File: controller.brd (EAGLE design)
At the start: 100 x 100 mm, 51 parts, among them IC1 7805DT, Q2 MOSFET-NCHANNELBSS123LT1G, Q3 MOSFET-NCHANNELFDD8780, U1 ATMEGA328P, Y1 16MHz

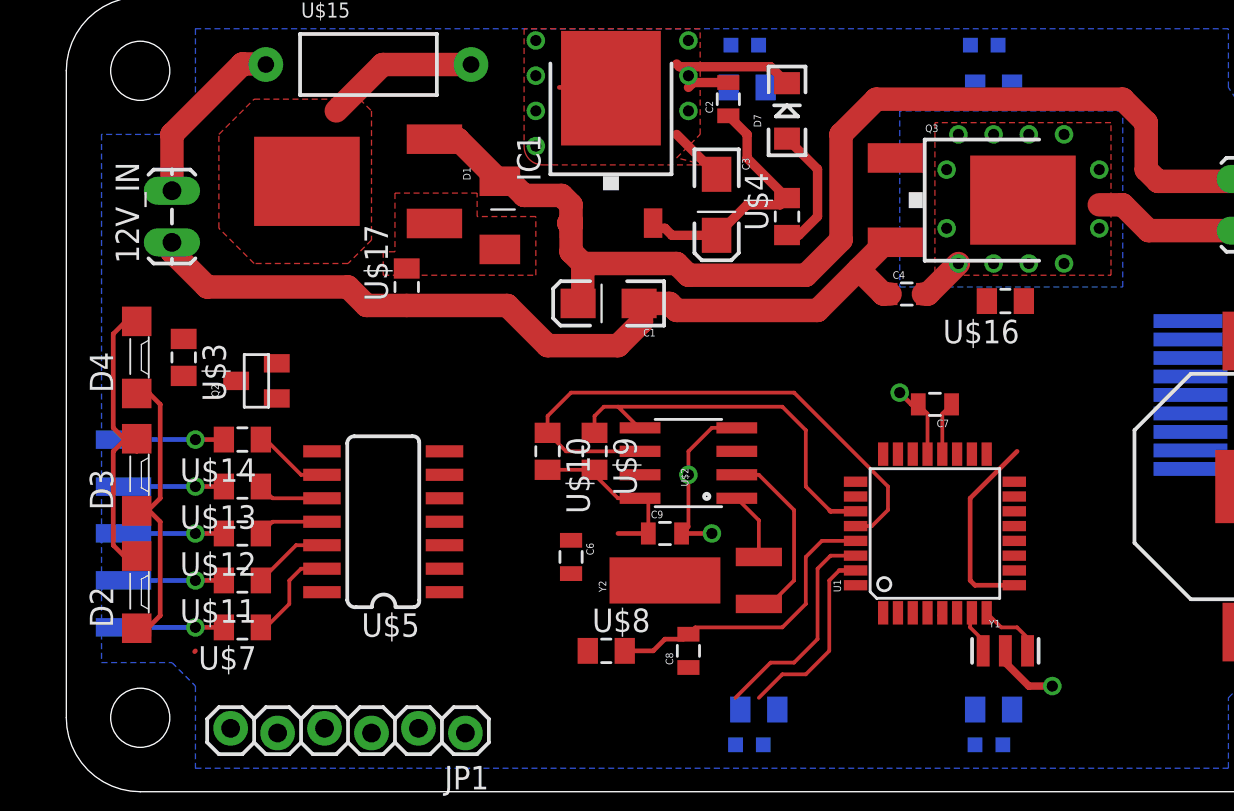
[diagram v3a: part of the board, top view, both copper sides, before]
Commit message: added current limit resistors. tightened rtc-mcu spacing.
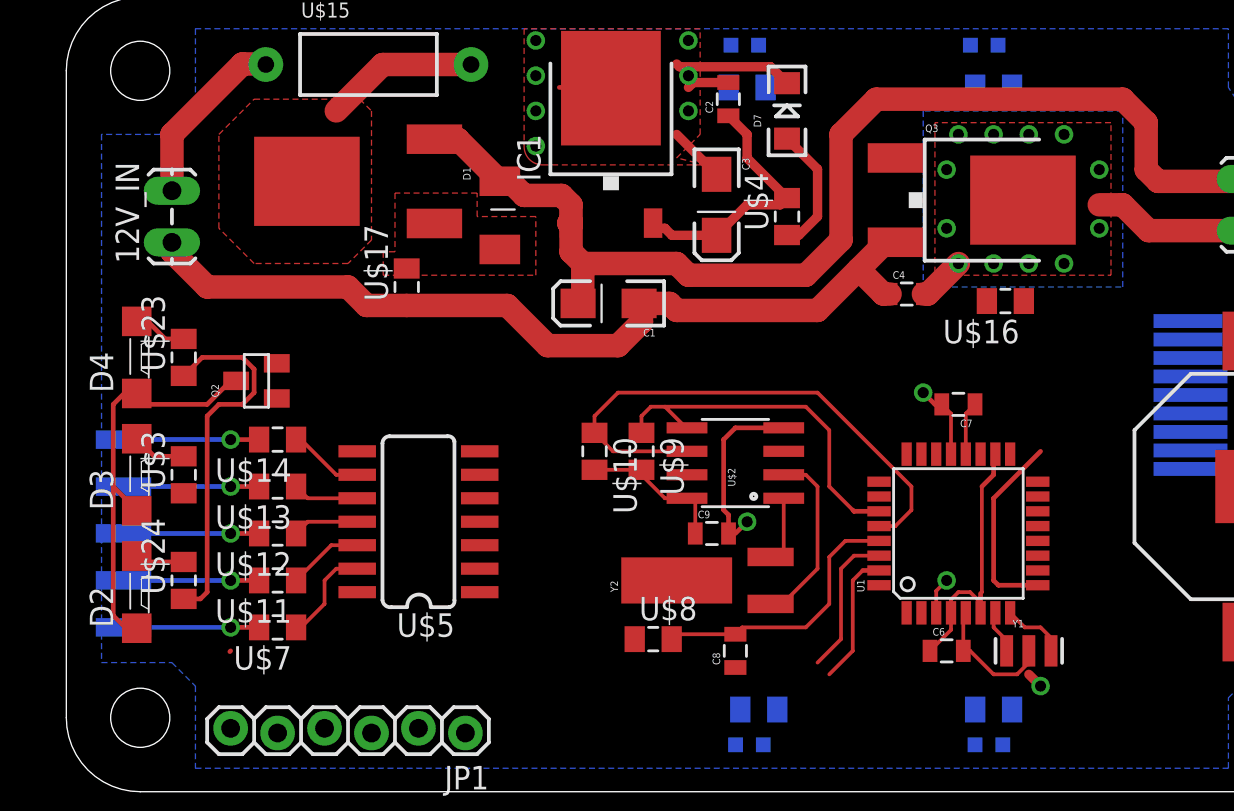
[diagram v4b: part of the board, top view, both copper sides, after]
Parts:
- added U$23, U$24: (no value), jt_parts:RESISTOR-0805
- moved C6 20.9 mm to (52.1, 11.4), turned to 0 degrees
- moved U$3 6.35 mm to (10.8, 21.0), turned to 90 degrees
- moved U$8 2.62 mm to (36.2, 12.1)
- moved U$10 2.54 mm to (33.0, 22.2)
- moved C8 2.54 mm to (40.6, 11.4)
- moved C9 2.54 mm to (39.4, 17.8)
- moved U$2 2.54 mm to (40.6, 21.6)
- moved U$9 2.54 mm to (35.6, 22.2)
- moved U$5 1.91 mm to (23.5, 17.8)
- moved U$11 1.90 mm to (15.9, 15.2)
- moved U$12 1.90 mm to (15.9, 17.8)
- moved U$13 1.90 mm to (15.9, 20.3)
- moved U$14 1.90 mm to (15.9, 22.9)
- moved U$7 1.90 mm to (15.9, 12.7)
- moved Y1 1.27 mm to (56.5, 11.4)
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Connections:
- removed net N$39: U$18.1, U$21.1, U$22.1, U$6.1
- new net N$36: D2.A, U$24.2
- new net N$37: D4.A, U$23.2
- net 12V: now also U$18.1, U$21.1, U$22.1, U$23.1, U$24.1, U$3.1, U$6.1
- net 5V: no longer U$3.1
- net N$9: no longer D2.A, D4.A
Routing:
- net 12V: track 62.9 -> 82.6 mm
- net N$9: track 17.0 -> 2.93 mm
- net 5V: track 23.9 -> 37.0 mm
- net GND: track 85.2 -> 91.7 mm
- net N$12: track 17.8 -> 22.5 mm
- net RXI: track 11.9 -> 7.96 mm
- net N$37: track 0.00 -> 3.38 mm
- net TXO: track 10.3 -> 7.25 mm
- net N$36: track 0.00 -> 2.67 mm
- net N$31: track 5.43 -> 7.33 mm
- net N$30: track 5.43 -> 7.33 mm
- net N$29: track 5.43 -> 7.33 mm
- net N$28: track 5.43 -> 7.33 mm
- net N$21: track 5.43 -> 7.33 mm
- net N$15: track 16.4 -> 14.9 mm
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
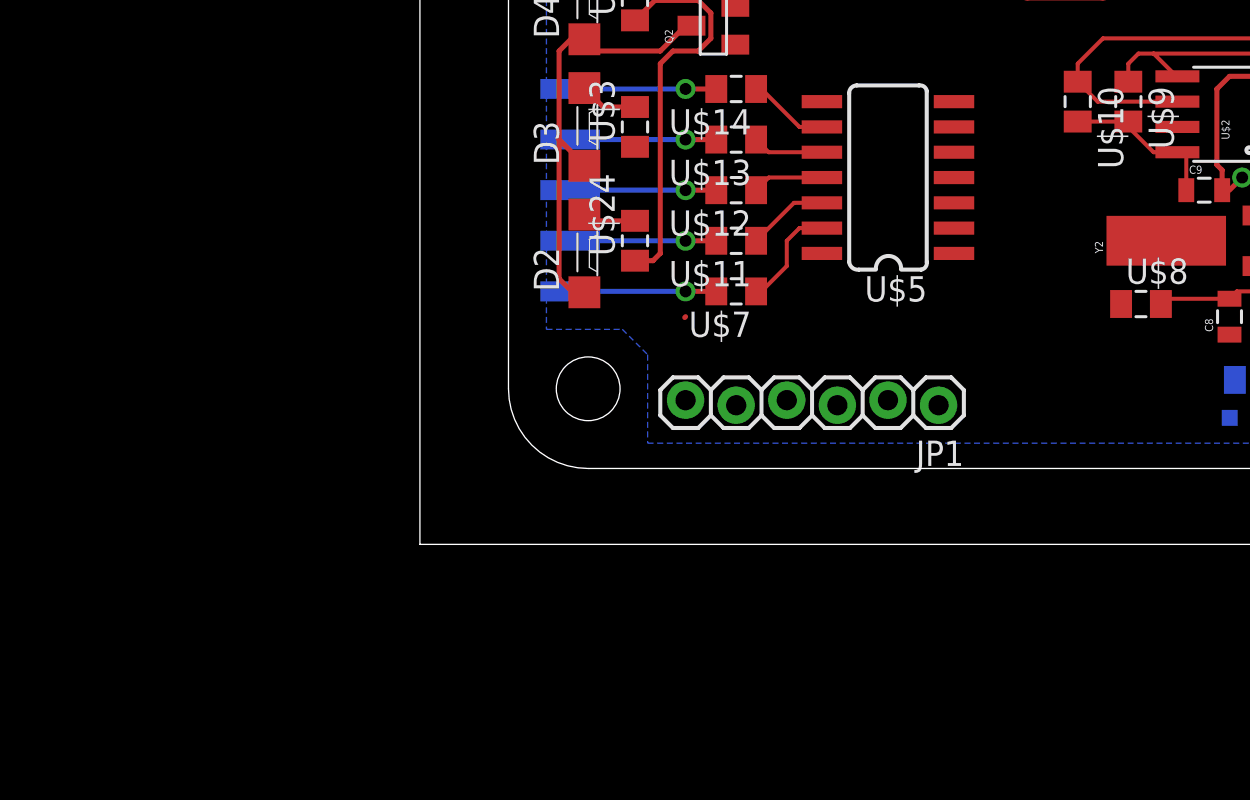
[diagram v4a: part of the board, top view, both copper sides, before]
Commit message: wired lcd for software reset.
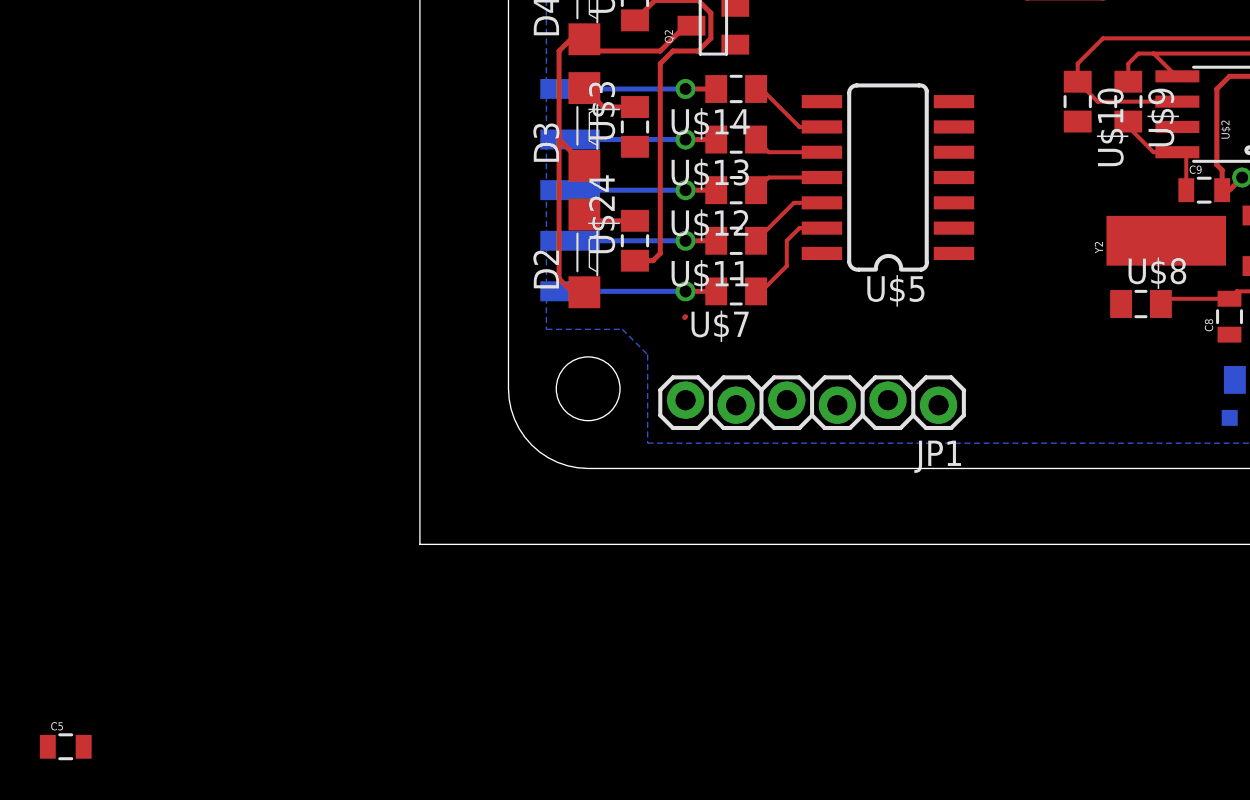
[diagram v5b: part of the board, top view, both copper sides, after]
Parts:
- added C5: (no value), SparkFun-Capacitors:0805
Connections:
- net N$17 renamed D/C
- net N$19 renamed /RES
- net N$2 renamed SDIN
- net N$5 renamed SCLK
- removed net N$18: NOKIA5110.5
- new net VCC: NOKIA5110.1, NOKIA5110.6, U$10.2, U$9.2
- net 5V: no longer NOKIA5110.1, U$10.2, U$9.2
- net GND: now also C5.1, NOKIA5110.5
- net N$20: now also C5.2, NOKIA5110.8; no longer NOKIA5110.6
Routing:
- net 5V: track 37.0 -> 34.2 mm
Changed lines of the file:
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@@
 <element name="U$23" library="jt_parts" package="RESISTOR-0805" value="" x="10.795" y="27.305" rot="R90"/>
 <element name="U$24" library="jt_parts" package="RESISTOR-0805" value="" x="10.795" y="15.24" rot="R90"/>
+<element name="C5" library="SparkFun-Capacitors" package="0805" value="" x="-17.78" y="-10.16"/>
 </elements>
 <signals>
@@
 <wire x1="51.505" y1="13.4874" x2="51.505" y2="14.675" width="0.2032" layer="1"/>
 <wire x1="51.505" y1="14.675" x2="52.07" y2="15.24" width="0.2032" layer="1"/>
-<wire x1="65.26" y1="23.273" x2="68.58" y2="20.32" width="0" layer="19" extent="1-16"/>
-<wire x1="40.27" y1="17.78" x2="40.64" y2="17.78" width="0" layer="19" extent="1-1"/>
-<wire x1="13.292" y1="11.387" x2="13.335" y2="7.239" width="0" layer="19" extent="1-1"/>
-<wire x1="15.832" y1="26.985" x2="12.065" y2="31.115" width="0" layer="19" extent="1-1"/>
-<wire x1="56.245" y1="30.353" x2="49.011" y2="30.734" width="0" layer="19" extent="1-1"/>
-<wire x1="26.8097" y1="14.605" x2="40.27" y2="17.78" width="0" layer="19" extent="1-1"/>
 <wire x1="43.2562" y1="23.495" x2="40.64" y2="23.495" width="0.254" layer="1"/>
 <wire x1="40.64" y1="23.495" x2="40.005" y2="22.86" width="0.254" layer="1"/>
@@
 <wire x1="40.27" y1="18.785" x2="40.005" y2="19.05" width="0.254" layer="1"/>
 <wire x1="57.15" y1="9.525" x2="56.515" y2="10.16" width="0.508" layer="1"/>
-<wire x1="56.515" y1="10.16" x2="56.1975" y2="10.4775" width="0" layer="19" extent="1-16"/>
+<contactref element="NOKIA5110" pad="5"/>
+<contactref element="C5" pad="1"/>
+<wire x1="43.434" y1="42.14" x2="54.852" y2="44.196" width="0" layer="19" extent="1-16"/>
+<wire x1="38.1" y1="42.545" x2="37.616" y2="43.029" width="0" layer="19" extent="1-1"/>
+<wire x1="38.365" y1="42.175" x2="38.1" y2="42.545" width="0" layer="19" extent="1-1"/>
+<wire x1="38.1" y1="40.64" x2="38.1" y2="41.91" width="0" layer="19" extent="1-1"/>
+<wire x1="41.898" y1="44.196" x2="42.545" y2="43.029" width="0" layer="19" extent="1-16"/>
+<wire x1="38.1" y1="44.45" x2="37.465" y2="43.18" width="0" layer="19" extent="1-1"/>
+<wire x1="37.465" y1="39.369" x2="38.1" y2="40.64" width="0" layer="19" extent="1-1"/>
+<wire x1="36.195" y1="39.37" x2="37.465" y2="39.369" width="0" layer="19" extent="1-1"/>
+<wire x1="29.845" y1="42.545" x2="31.115" y2="41.91" width="0" layer="19" extent="1-1"/>
+<wire x1="29.845" y1="40.64" x2="31.115" y2="41.91" width="0" layer="19" extent="1-1"/>
+<wire x1="29.845" y1="44.45" x2="29.845" y2="42.545" width="0" layer="19" extent="1-1"/>
+<wire x1="29.845" y1="38.735" x2="29.845" y2="40.64" width="0" layer="19" extent="1-1"/>
+<wire x1="37.084" y1="30.226" x2="39.624" y2="37.21" width="0" layer="19" extent="1-1"/>
+<wire x1="15.832" y1="26.985" x2="12.065" y2="31.115" width="0" layer="19" extent="1-1"/>
+<wire x1="50.8" y1="25.4" x2="49.011" y2="30.734" width="0" layer="19" extent="1-1"/>
+<wire x1="43.2562" y1="23.495" x2="45.085" y2="29.845" width="0" layer="19" extent="1-1"/>
+<wire x1="40.64" y1="17.78" x2="40.27" y2="17.78" width="0" layer="19" extent="1-1"/>
+<wire x1="52.07" y1="15.24" x2="52.305" y2="22.0726" width="0" layer="19" extent="1-1"/>
+<wire x1="52.97" y1="13.3524" x2="51.505" y2="13.4874" width="0" layer="19" extent="1-1"/>
+<wire x1="56.515" y1="10.16" x2="56.515" y2="10.795" width="0" layer="19" extent="1-1"/>
+<wire x1="55.106" y1="6.35" x2="57.15" y2="9.525" width="0" layer="19" extent="16-16"/>
+<wire x1="56.245" y1="30.353" x2="51.805" y2="24.765" width="0" layer="19" extent="1-1"/>
+<wire x1="65.26" y1="25.273" x2="56.245" y2="30.353" width="0" layer="19" extent="1-16"/>
+<wire x1="65.26" y1="23.273" x2="65.26" y2="25.273" width="0" layer="19" extent="16-16"/>
+<wire x1="68.58" y1="20.32" x2="65.26" y2="23.273" width="0" layer="19" extent="1-16"/>
+<wire x1="42.152" y1="6.35" x2="40.64" y2="17.78" width="0" layer="19" extent="1-16"/>
+<wire x1="26.8097" y1="14.605" x2="30.48" y2="27.94" width="0" layer="19" extent="1-1"/>
+<wire x1="15.875" y1="6.985" x2="26.8097" y2="14.605" width="0" layer="19" extent="1-1"/>
+<wire x1="13.335" y1="7.239" x2="15.875" y2="6.985" width="0" layer="19" extent="1-1"/>
+<wire x1="13.292" y1="11.387" x2="13.335" y2="7.239" width="0" layer="19" extent="1-1"/>
+<wire x1="-18.68" y1="-10.16" x2="13.335" y2="7.239" width="0" layer="19" extent="1-1"/>
 </signal>
 <signal name="5V" class="2">
@@
 <contactref element="C9" pad="1"/>
 <contactref element="U$2" pad="8"/>
-<contactref element="U$9" pad="2"/>
-<contactref element="U$10" pad="2"/>
-<wire x1="33.02" y1="21.225" x2="35.56" y2="21.225" width="0.2032" layer="1"/>
-<wire x1="35.56" y1="21.225" x2="35.56" y2="20.955" width="0.2032" layer="1"/>
 <wire x1="35.56" y1="20.955" x2="36.83" y2="19.685" width="0.2032" layer="1"/>
 <wire x1="36.83" y1="19.685" x2="38.0238" y2="19.685" width="0.2032" layer="1"/>
 <wire x1="38.0238" y1="19.685" x2="38.47" y2="19.685" width="0.2032" layer="1"/>
 <wire x1="38.47" y1="19.685" x2="38.47" y2="17.78" width="0.2032" layer="1"/>
-<contactref element="NOKIA5110" pad="1"/>
 <wire x1="40.259" y1="40.375" x2="40.27" y2="40.375" width="0.508" layer="1"/>
 <wire x1="40.27" y1="40.375" x2="41.275" y2="39.37" width="0.508" layer="1"/>
@@
 <wire x1="54.61" y1="20.955" x2="54.61" y2="21.9776" width="0.254" layer="1"/>
 <wire x1="54.61" y1="21.9776" x2="54.705" y2="22.0726" width="0.2032" layer="1"/>
-<wire x1="54.705" y1="22.0726" x2="65.26" y2="29.273" width="0" layer="19" extent="1-16"/>
-<wire x1="38.47" y1="17.78" x2="51.17" y2="11.43" width="0" layer="19" extent="1-1"/>
-<wire x1="35.195" y1="12.065" x2="38.47" y2="17.78" width="0" layer="19" extent="1-1"/>
-<wire x1="20.1803" y1="14.605" x2="33.02" y2="21.225" width="0" layer="19" extent="1-1"/>
-<wire x1="18.415" y1="7.239" x2="20.1803" y2="14.605" width="0" layer="19" extent="1-1"/>
-<wire x1="37.21" y1="33.91" x2="35.56" y2="21.225" width="0" layer="19" extent="1-1"/>
 <wire x1="52.305" y1="13.4874" x2="52.305" y2="12.565" width="0.2032" layer="1"/>
 <wire x1="52.305" y1="12.565" x2="51.17" y2="11.43" width="0.2032" layer="1"/>
+<wire x1="35.56" y1="20.955" x2="37.21" y2="33.91" width="0" layer="19" extent="1-1"/>
+<wire x1="35.195" y1="12.065" x2="38.47" y2="17.78" width="0" layer="19" extent="1-1"/>
+<wire x1="51.17" y1="11.43" x2="38.47" y2="17.78" width="0" layer="19" extent="1-1"/>
+<wire x1="20.1803" y1="14.605" x2="35.195" y2="12.065" width="0" layer="19" extent="1-1"/>
+<wire x1="18.415" y1="7.239" x2="20.1803" y2="14.605" width="0" layer="19" extent="1-1"/>
 </signal>
 <signal name="N$64">
@@
 </polygon>
 </signal>
-<signal name="N$2">
+<signal name="SDIN">
 <contactref element="NOKIA5110" pad="3"/>
 </signal>
-<signal name="N$5">
+<signal name="SCLK">
 <contactref element="NOKIA5110" pad="2"/>
 </signal>
-<signal name="N$17">
+<signal name="D/C">
 <contactref element="NOKIA5110" pad="4"/>
 </signal>
-<signal name="N$18">
-<contactref element="NOKIA5110" pad="5"/>
-</signal>
-<signal name="N$19">
+<signal name="/RES">
 <contactref element="NOKIA5110" pad="9"/>
-</signal>
-<signal name="N$20">
-<contactref element="NOKIA5110" pad="6"/>
 </signal>
 <signal name="PWM_LED">
@@
 <wire x1="8.3" y1="29.21" x2="8.255" y2="29.255" width="0.254" layer="1"/>
 </signal>
+<signal name="N$20">
+<contactref element="NOKIA5110" pad="8"/>
+<contactref element="C5" pad="2"/>
+<wire x1="-16.88" y1="-10.16" x2="65.26" y2="22.273" width="0" layer="19" extent="1-16"/>
+</signal>
+<signal name="VCC">
+<contactref element="U$9" pad="2"/>
+<contactref element="U$10" pad="2"/>
+<contactref element="NOKIA5110" pad="1"/>
+<contactref element="NOKIA5110" pad="6"/>
+<wire x1="65.26" y1="24.273" x2="65.26" y2="29.273" width="0" layer="19" extent="16-16"/>
+<wire x1="35.56" y1="21.225" x2="65.26" y2="24.273" width="0" layer="19" extent="1-16"/>
+<wire x1="33.02" y1="21.225" x2="35.56" y2="21.225" width="0" layer="19" extent="1-1"/>
+</signal>
 </signals>
